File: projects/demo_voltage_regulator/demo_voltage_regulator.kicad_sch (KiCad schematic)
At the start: 7 parts, among them U1 LM7805

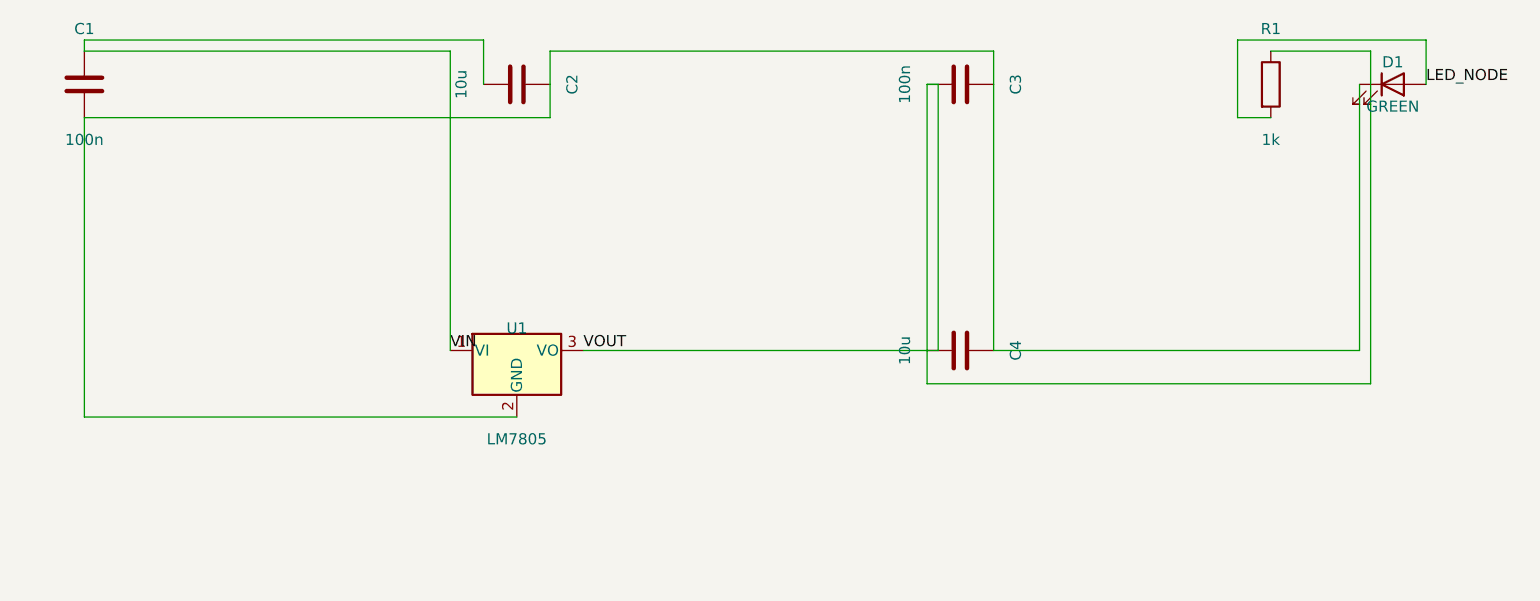
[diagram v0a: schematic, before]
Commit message: Phase 0: KiCad 10 migration + fix blind ERC parsing
- kicad-cli writes JSON reports only to -o file, never stdout; runner
  now uses a temp report file and real JSON decoding
- DetectKicadCLI exported and reused by render_sch and export_test
- KiCad 10 symbol renames (ATmega328-AU -> ATmega328-A) and pin
  numbers fixed in demos

Co-Authored-By: Claude Fable 5 <noreply@anthropic.com>
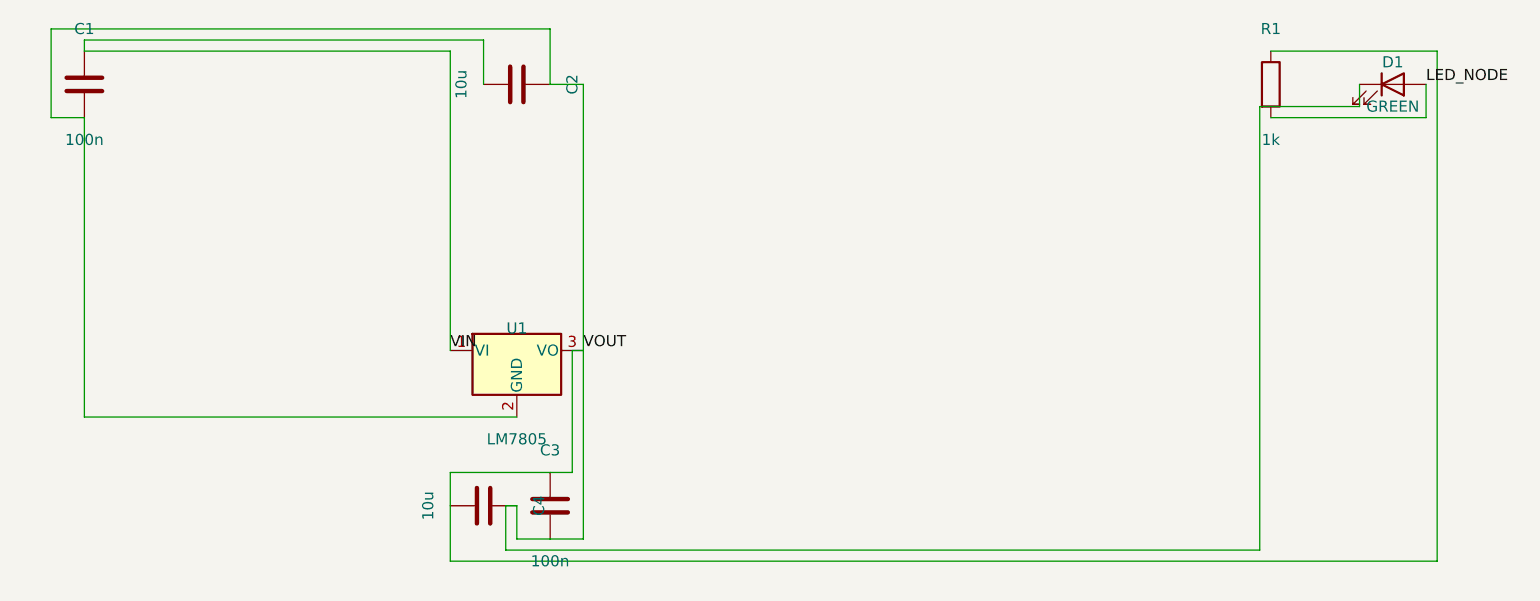
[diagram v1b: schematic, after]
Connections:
- net VOUT: now also C1.2, C2.2, C3.2, C4.2, D1.1 (K), U1.2 (GND)

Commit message: Phase 1: geometric quality gate (internal/place2/gate)
Post-hoc Enforce() guarantees zero cross-net crossings, zero wires
through symbol bodies, zero collinear overlaps: offending nets are
demoted to net labels (no geometry, identical connectivity). Wired
into connect_netlist and relayout. Same-net duplicate segments are
merged by Clean, not demoted.

Co-Authored-By: Claude Fable 5 <noreply@anthropic.com>
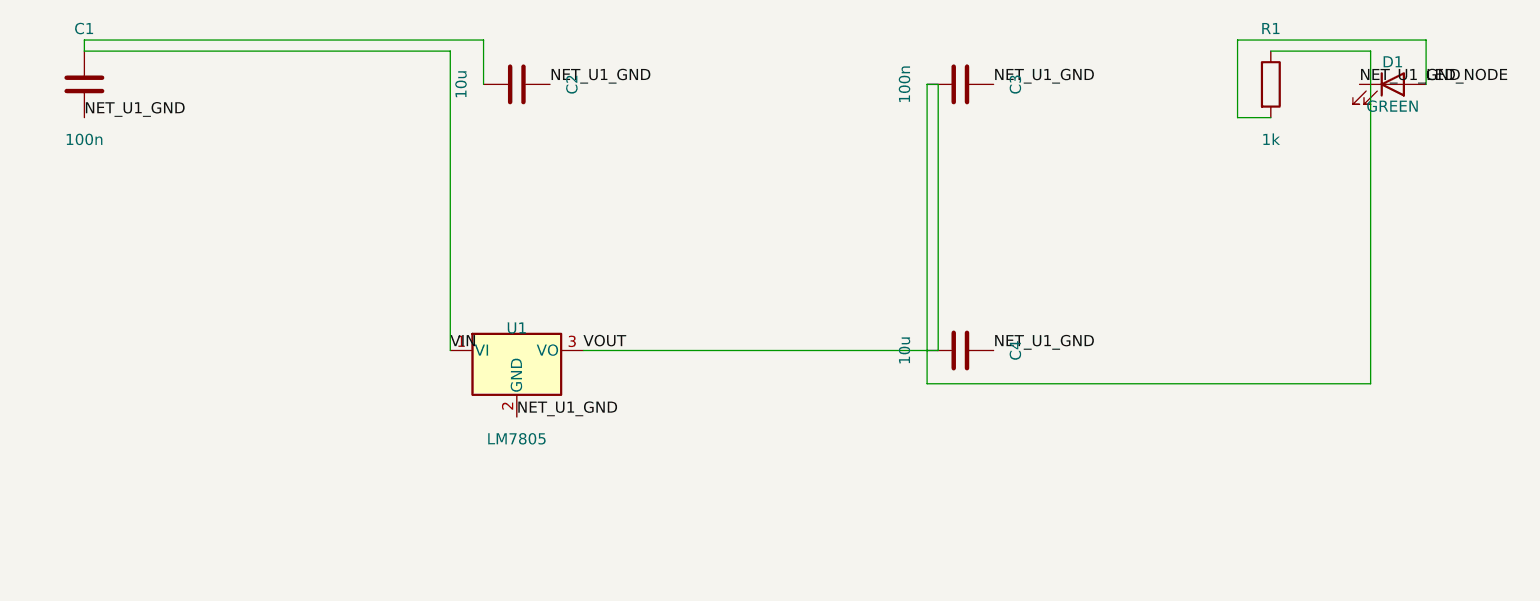
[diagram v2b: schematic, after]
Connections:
- net VOUT: no longer C1.2, C2.2, C3.2, C4.2, D1.1 (K), U1.2 (GND)
- new net NET_U1_GND: C1.2, C2.2, C3.2, C4.2, D1.1 (K), U1.2 (GND)

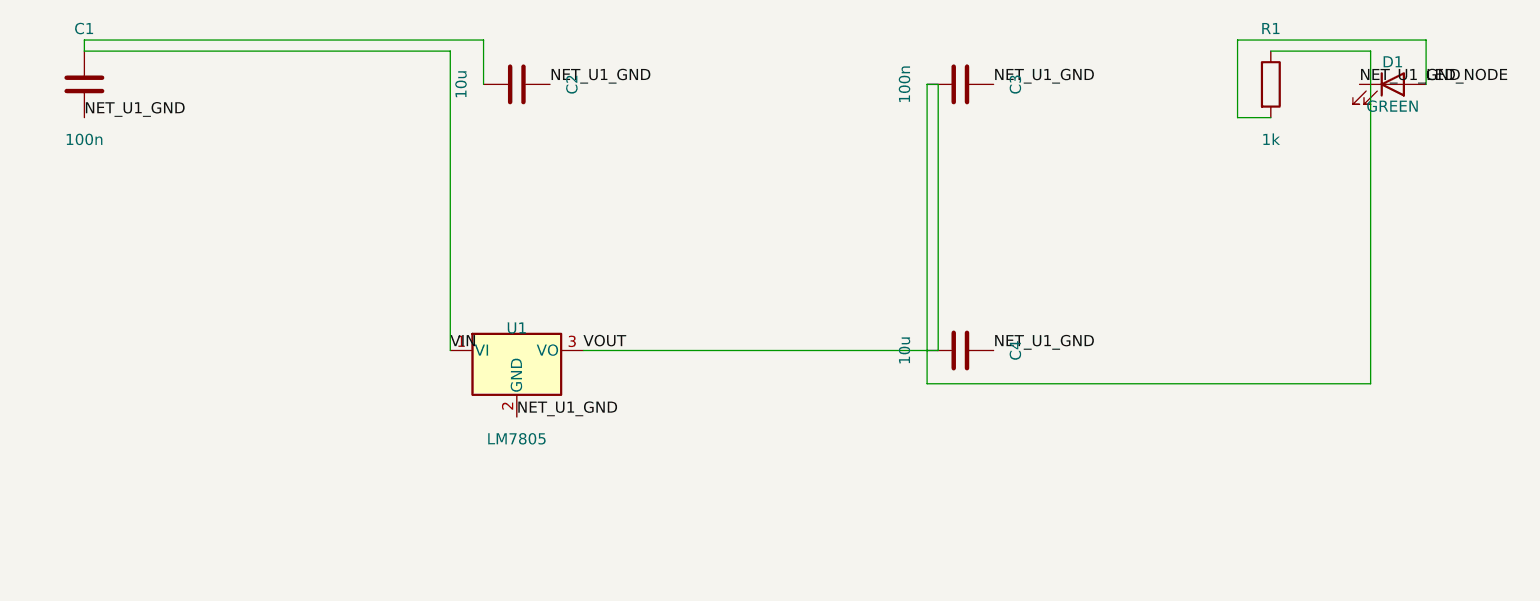
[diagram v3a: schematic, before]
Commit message: Phase 4: per-pin power rail policy + full pipeline determinism
Power nets are never routed: every pin on a rail gets its own power
symbol (GND down, VCC up) with a 2.54mm stub; PWR_FLAG emitted after
the gate for undriven power_in nets. Determinism: cluster detection
and TraceNets no longer depend on Go map iteration order (refOrder
slices, sorted canonical net naming). 6/6 identical runs on vreg and
mcu demos; vreg ERC now has zero errors.

Co-Authored-By: Claude Fable 5 <noreply@anthropic.com>
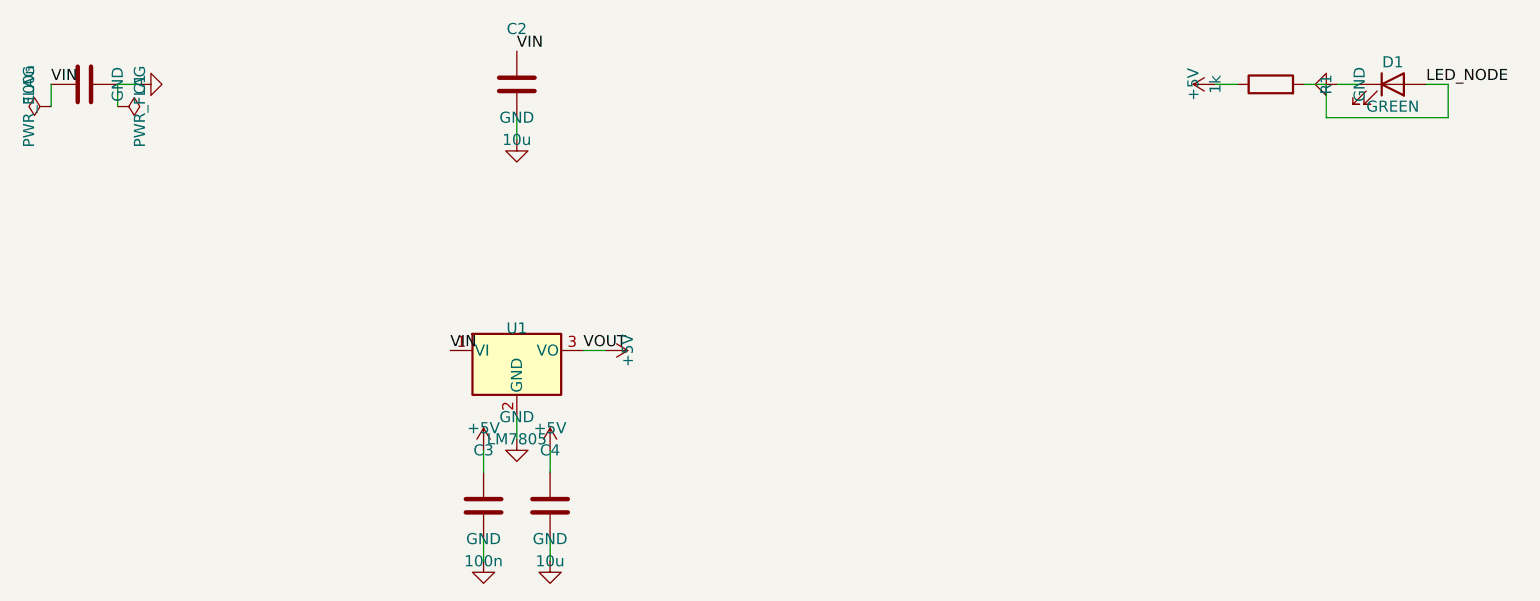
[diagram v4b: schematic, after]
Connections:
- net NET_U1_GND renamed GND
- net VOUT renamed +5V
